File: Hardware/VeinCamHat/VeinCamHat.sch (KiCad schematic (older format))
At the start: 23 parts, among them J1 Raspberry_Pi_2_3, Q1 NTJD4001N

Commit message: More schematic / PCB changes
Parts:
- R2: value 1k -> 1k5
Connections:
- net +3V3: now also D2.2 (A), J1.17 (3V3)
- net GND: now also R2.2; no longer D2.1 (K)
- net LED_READY: now also J1.37 (GPIO26), R1.2; no longer J1.7 (GCLK0/GPIO4), R1.1
- net at D1.2 (A): now also R1.1; no longer R1.2
- net nLED_BOOT: now reaches J1.35 (GPIO19/MISO1)
- net nLED_BOOT: now also D2.1 (K), R2.1
- net LED_BOOT: no longer names the net of J1.8 (GPIO14/TXD)
- net LED_BOOT: no longer R2.1
- no-connect marks 28 -> 27
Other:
- moved on the sheet: D1, D2, R1, R2
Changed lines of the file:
@@
 EESchema Schematic File Version 4
 LIBS:VeinCamHat-cache
-EELAYER 26 0
+EELAYER 29 0
 EELAYER END
 $Descr A4 11693 8268
@@
 L Device:R R1
 U 1 1 5D25BF6E
-P 4100 1800
-F 0 "R1" V 4200 1750 50  0000 L CNN
-F 1 "1k" V 4000 1750 50  0000 L CNN
-F 2 "Resistor_SMD:R_0603_1608Metric" V 4030 1800 50  0001 C CNN
-F 3 "~" H 4100 1800 50  0001 C CNN
-	1    4100 1800
-	0    -1   -1   0
+P 4150 1900
+F 0 "R1" V 4050 1850 50  0000 L CNN
+F 1 "1k" V 4250 1850 50  0000 L CNN
+F 2 "Resistor_SMD:R_0603_1608Metric" V 4080 1900 50  0001 C CNN
+F 3 "~" H 4150 1900 50  0001 C CNN
+	1    4150 1900
+	0    1    1    0
 $EndComp
 $Comp
 L Device:LED D1
 U 1 1 5D25BF75
-P 4450 1800
-F 0 "D1" H 4500 1700 50  0000 R CNN
-F 1 "GREEN LED" H 4650 1900 50  0000 R CNN
-F 2 "LED_SMD:LED_0805_2012Metric" H 4450 1800 50  0001 C CNN
-F 3 "~" H 4450 1800 50  0001 C CNN
-	1    4450 1800
+P 4550 1900
+F 0 "D1" H 4600 1800 50  0000 R CNN
+F 1 "GREEN LED" H 4750 2000 50  0000 R CNN
+F 2 "LED_SMD:LED_0805_2012Metric" H 4550 1900 50  0001 C CNN
+F 3 "~" H 4550 1900 50  0001 C CNN
+	1    4550 1900
 	-1   0    0    1
-$EndComp
-$Comp
-L power:GND #PWR04
-U 1 1 5D25BF7C
-P 4850 1850
-F 0 "#PWR04" H 4850 1600 50  0001 C CNN
-F 1 "GND" H 4855 1677 50  0000 C CNN
-F 2 "" H 4850 1850 50  0001 C CNN
-F 3 "" H 4850 1850 50  0001 C CNN
-	1    4850 1850
-	1    0    0    -1
-$EndComp
-Wire Wire Line
-	4300 1800 4250 1800
-$Comp
-L Connector:Raspberry_Pi_2_3 J1
-U 1 1 5D30B49A
-P 1850 2550
-F 0 "J1" H 1200 3900 50  0000 C CNN
-F 1 "Raspberry_Pi_2_3" H 1250 3800 50  0000 C CNN
-F 2 "Connector_PinSocket_2.54mm:PinSocket_2x20_P2.54mm_Vertical" H 1850 2550 50  0001 C CNN
-F 3 "https://www.raspberrypi.org/documentation/hardware/raspberrypi/schematics/rpi_SCH_3bplus_1p0_reduced.pdf" H 1850 2550 50  0001 C CNN
-	1    1850 2550
-	1    0    0    -1
 $EndComp
 Wire Wire Line
@@
 	10450 2350 10450 2750
 Connection ~ 10450 2350
-Text Label 3100 2250 2    50   ~ 0
+Text Label 600  3150 0    50   ~ 0
 LED_READY
 Wire Wire Line
-	3100 2250 2650 2250
-Wire Wire Line
-	600  1650 1050 1650
-Text Label 600  1650 0    50   ~ 0
-LED_BOOT
-Text Label 3500 1800 0    50   ~ 0
+	600  3150 1050 3150
+Wire Wire Line
+	600  2350 1050 2350
+Text Label 600  2350 0    50   ~ 0
+nLED_BOOT
+Text Label 3500 1900 0    50   ~ 0
 LED_READY
-Text Label 3500 2250 0    50   ~ 0
-LED_BOOT
-Wire Wire Line
-	3500 1800 3950 1800
-Wire Wire Line
-	4850 1800 4850 1850
-Wire Wire Line
-	4600 1800 4850 1800
+Text Label 3500 2550 0    50   ~ 0
+nLED_BOOT
 $Comp
 L Device:R R2
 U 1 1 5D6666C3
-P 4100 2250
-F 0 "R2" V 4200 2200 50  0000 L CNN
-F 1 "1k" V 4000 2200 50  0000 L CNN
-F 2 "Resistor_SMD:R_0603_1608Metric" V 4030 2250 50  0001 C CNN
-F 3 "~" H 4100 2250 50  0001 C CNN
-	1    4100 2250
-	0    -1   -1   0
+P 4100 2800
+F 0 "R2" H 4150 2850 50  0000 L CNN
+F 1 "1k5" H 4150 2750 50  0000 L CNN
+F 2 "Resistor_SMD:R_0603_1608Metric" V 4030 2800 50  0001 C CNN
+F 3 "~" H 4100 2800 50  0001 C CNN
+	1    4100 2800
+	1    0    0    -1
 $EndComp
 $Comp
 L Device:LED D2
 U 1 1 5D6666CA
-P 4450 2250
-F 0 "D2" H 4500 2150 50  0000 R CNN
-F 1 "RED LED" H 4650 2350 50  0000 R CNN
-F 2 "LED_SMD:LED_0805_2012Metric" H 4450 2250 50  0001 C CNN
-F 3 "~" H 4450 2250 50  0001 C CNN
-	1    4450 2250
-	-1   0    0    1
-$EndComp
-$Comp
-L power:GND #PWR05
-U 1 1 5D6666D1
-P 4850 2300
-F 0 "#PWR05" H 4850 2050 50  0001 C CNN
-F 1 "GND" H 4855 2127 50  0000 C CNN
-F 2 "" H 4850 2300 50  0001 C CNN
-F 3 "" H 4850 2300 50  0001 C CNN
-	1    4850 2300
-	1    0    0    -1
-$EndComp
-Wire Wire Line
-	4300 2250 4250 2250
-Wire Wire Line
-	3500 2250 3950 2250
-Wire Wire Line
-	4850 2250 4850 2300
-Wire Wire Line
-	4600 2250 4850 2250
+P 4400 2550
+F 0 "D2" H 4450 2650 50  0000 R CNN
+F 1 "RED LED" H 4650 2450 50  0000 R CNN
+F 2 "LED_SMD:LED_0805_2012Metric" H 4400 2550 50  0001 C CNN
+F 3 "~" H 4400 2550 50  0001 C CNN
+	1    4400 2550
+	1    0    0    -1
+$EndComp
 $Comp
 L VeinCam_Symbols:SFH7252 D3
@@
 NoConn ~ 1050 1950
 NoConn ~ 1050 2050
-NoConn ~ 1050 2350
 NoConn ~ 1050 2450
 NoConn ~ 1050 2550
 NoConn ~ 1050 2950
 NoConn ~ 1050 3050
-NoConn ~ 1050 3150
 NoConn ~ 1050 3250
 NoConn ~ 2650 3050
@@
 NoConn ~ 1050 2850
 NoConn ~ 2650 3250
-NoConn ~ 1950 1250
-NoConn ~ 2050 1250
 NoConn ~ 12400 3300
 NoConn ~ 1050 2750
@@
 	1    0    0    -1
 $EndComp
+$Comp
+L power:+3V3 #PWR0101
+U 1 1 5CB9F567
+P 2050 1150
+F 0 "#PWR0101" H 2050 1000 50  0001 C CNN
+F 1 "+3V3" H 2065 1323 50  0000 C CNN
+F 2 "" H 2050 1150 50  0001 C CNN
+F 3 "" H 2050 1150 50  0001 C CNN
+	1    2050 1150
+	1    0    0    -1
+$EndComp
+$Comp
+L power:+3V3 #PWR0103
+U 1 1 5CBA5562
+P 4900 2500
+F 0 "#PWR0103" H 4900 2350 50  0001 C CNN
+F 1 "+3V3" H 4915 2673 50  0000 C CNN
+F 2 "" H 4900 2500 50  0001 C CNN
+F 3 "" H 4900 2500 50  0001 C CNN
+	1    4900 2500
+	1    0    0    -1
+$EndComp
+Wire Wire Line
+	4900 2500 4900 2550
+Wire Wire Line
+	4550 2550 4900 2550
+Wire Wire Line
+	4700 1900 4900 1900
+Wire Wire Line
+	4100 2950 4100 3000
+$Comp
+L power:GND #PWR0104
+U 1 1 5CBB9F2E
+P 4100 3000
+F 0 "#PWR0104" H 4100 2750 50  0001 C CNN
+F 1 "GND" H 4105 2827 50  0000 C CNN
+F 2 "" H 4100 3000 50  0001 C CNN
+F 3 "" H 4100 3000 50  0001 C CNN
+	1    4100 3000
+	1    0    0    -1
+$EndComp
+$Comp
+L Connector:Raspberry_Pi_2_3 J1
+U 1 1 5D30B49A
+P 1850 2550
+F 0 "J1" H 1200 3900 50  0000 C CNN
+F 1 "Raspberry_Pi_2_3" H 1250 3800 50  0000 C CNN
+F 2 "Connector_PinSocket_2.54mm:PinSocket_2x20_P2.54mm_Vertical" H 1850 2550 50  0001 C CNN
+F 3 "https://www.raspberrypi.org/documentation/hardware/raspberrypi/schematics/rpi_SCH_3bplus_1p0_reduced.pdf" H 1850 2550 50  0001 C CNN
+	1    1850 2550
+	1    0    0    -1
+$EndComp
+Wire Wire Line
+	2050 1150 2050 1250
+NoConn ~ 1950 1250
+$Comp
+L power:GND #PWR0102
+U 1 1 5CC02B04
+P 4900 1950
+F 0 "#PWR0102" H 4900 1700 50  0001 C CNN
+F 1 "GND" H 4905 1777 50  0000 C CNN
+F 2 "" H 4900 1950 50  0001 C CNN
+F 3 "" H 4900 1950 50  0001 C CNN
+	1    4900 1950
+	1    0    0    -1
+$EndComp
+Wire Wire Line
+	4900 1900 4900 1950
+Wire Wire Line
+	3500 1900 4000 1900
+Wire Wire Line
+	4300 1900 4400 1900
+Wire Wire Line
+	3500 2550 4100 2550
+Wire Wire Line
+	4100 2650 4100 2550
+Connection ~ 4100 2550
+Wire Wire Line
+	4100 2550 4250 2550
+NoConn ~ 1050 1650
+NoConn ~ 2650 2250
 $EndSCHEMATC

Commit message: updated schematic
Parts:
- R1: value 1k -> 1K
- R2: value 1k5 -> 1K5
- R7, R8: value 10k -> 10K
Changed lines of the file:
@@
 P 8600 3150
 F 0 "R7" H 8670 3196 50  0000 L CNN
-F 1 "10k" H 8670 3105 50  0000 L CNN
+F 1 "10K" H 8670 3105 50  0000 L CNN
 F 2 "Resistor_SMD:R_0603_1608Metric" V 8530 3150 50  0001 C CNN
 F 3 "~" H 8600 3150 50  0001 C CNN
@@
 P 10050 3150
 F 0 "R8" H 10120 3196 50  0000 L CNN
-F 1 "10k" H 10120 3105 50  0000 L CNN
+F 1 "10K" H 10120 3105 50  0000 L CNN
 F 2 "Resistor_SMD:R_0603_1608Metric" V 9980 3150 50  0001 C CNN
 F 3 "~" H 10050 3150 50  0001 C CNN
@@
 P 4150 1900
 F 0 "R1" V 4050 1850 50  0000 L CNN
-F 1 "1k" V 4250 1850 50  0000 L CNN
+F 1 "1K" V 4250 1850 50  0000 L CNN
 F 2 "Resistor_SMD:R_0603_1608Metric" V 4080 1900 50  0001 C CNN
 F 3 "~" H 4150 1900 50  0001 C CNN
@@
 P 4100 2800
 F 0 "R2" H 4150 2850 50  0000 L CNN
-F 1 "1k5" H 4150 2750 50  0000 L CNN
+F 1 "1K5" H 4150 2750 50  0000 L CNN
 F 2 "Resistor_SMD:R_0603_1608Metric" V 4030 2800 50  0001 C CNN
 F 3 "~" H 4100 2800 50  0001 C CNN

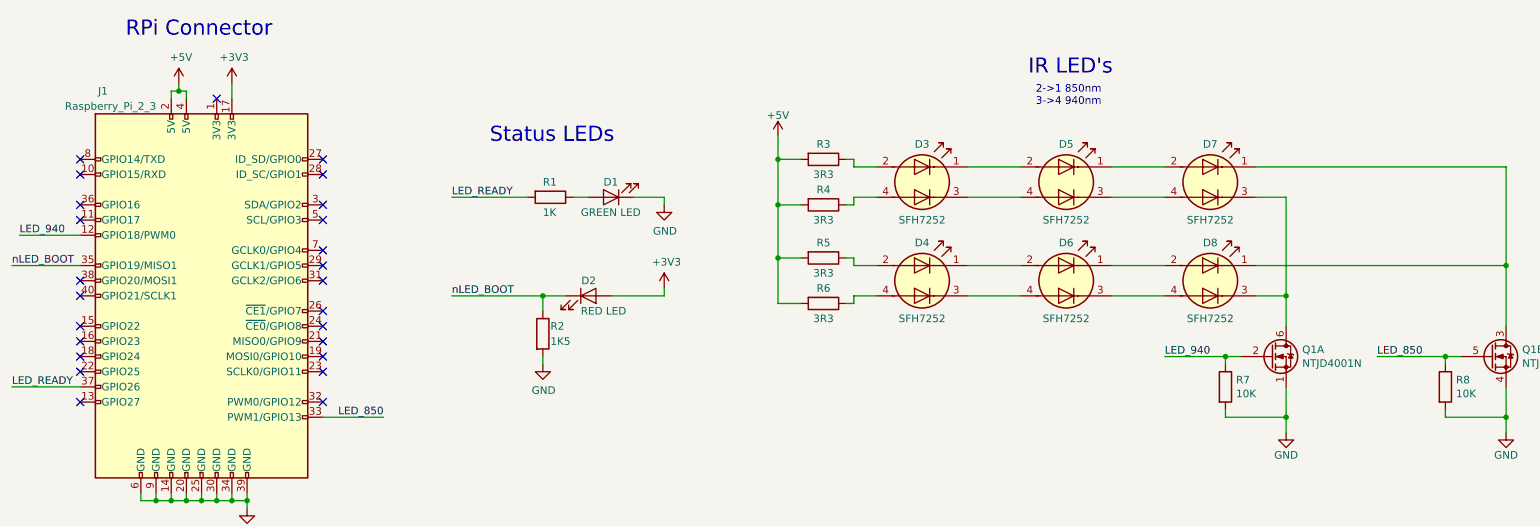
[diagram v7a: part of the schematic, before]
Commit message: Josh can't read datasheets correctly
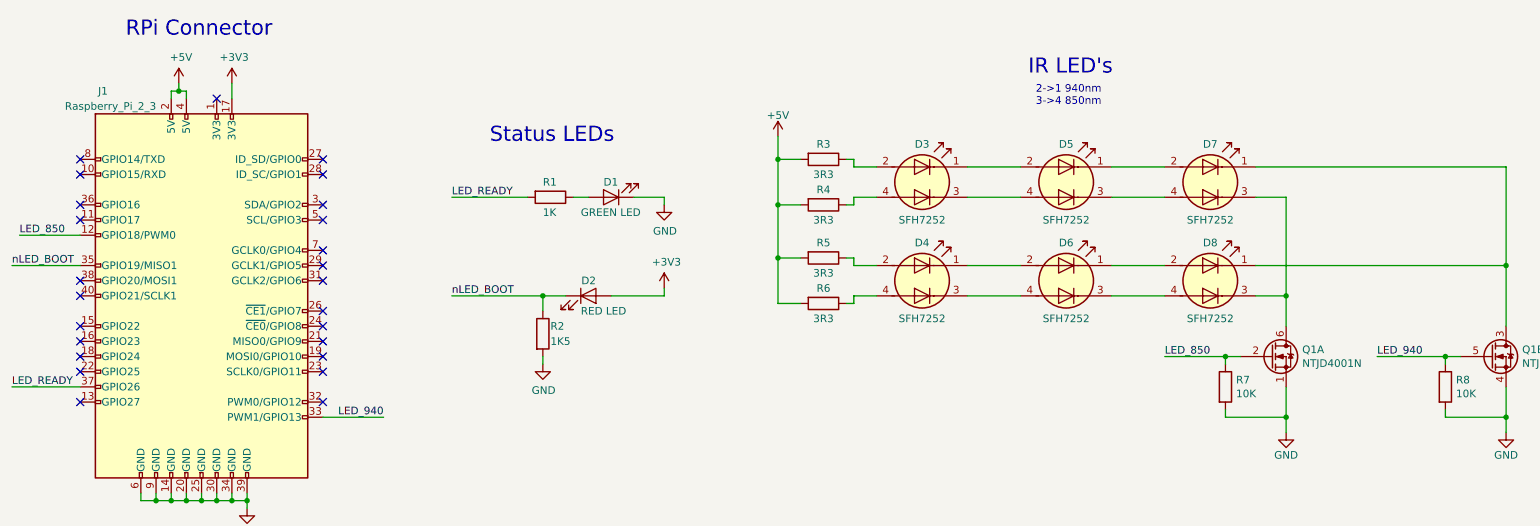
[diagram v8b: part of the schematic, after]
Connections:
- net LED_850: now also J1.12 (GPIO18/PWM0), Q1.2 (G), R7.1; no longer J1.33 (PWM1/GPIO13), Q1.5 (G), R8.1
- net LED_940: now also J1.33 (PWM1/GPIO13), Q1.5 (G), R8.1; no longer J1.12 (GPIO18/PWM0), Q1.2 (G), R7.1
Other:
- note added: "2->1 940nm\n3->4 850nm"
- note removed: "2->1 850nm\n3->4 940nm"
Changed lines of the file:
@@
 	8800 2350 10450 2350
 Text Notes 7350 1300 0    50   ~ 0
-2->1 850nm\n3->4 940nm
+2->1 940nm\n3->4 850nm
 Text Notes 3750 1550 0    100  ~ 0
 Status LEDs
@@
 Wire Wire Line
 	2650 3350 3050 3350
+Text Label 3050 3350 2    50   ~ 0
+LED_940
 Text Label 650  2150 0    50   ~ 0
-LED_940
-Text Label 3050 3350 2    50   ~ 0
 LED_850
-Text Label 9600 2950 0    50   ~ 0
+Text Label 8200 2950 0    50   ~ 0
 LED_850
 Wire Wire Line
 	8600 2950 8200 2950
 Connection ~ 8600 2950
-Text Label 8200 2950 0    50   ~ 0
+Text Label 9600 2950 0    50   ~ 0
 LED_940
 Wire Wire Line
